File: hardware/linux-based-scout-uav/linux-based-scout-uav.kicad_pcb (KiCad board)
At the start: 2 copper layers, 39.4 x 59.1 mm, 3 parts, among them J1 XT60PW-M, J2 Micro_SD_Card_Det2, U1 OSD32MP157C-512M-IAA

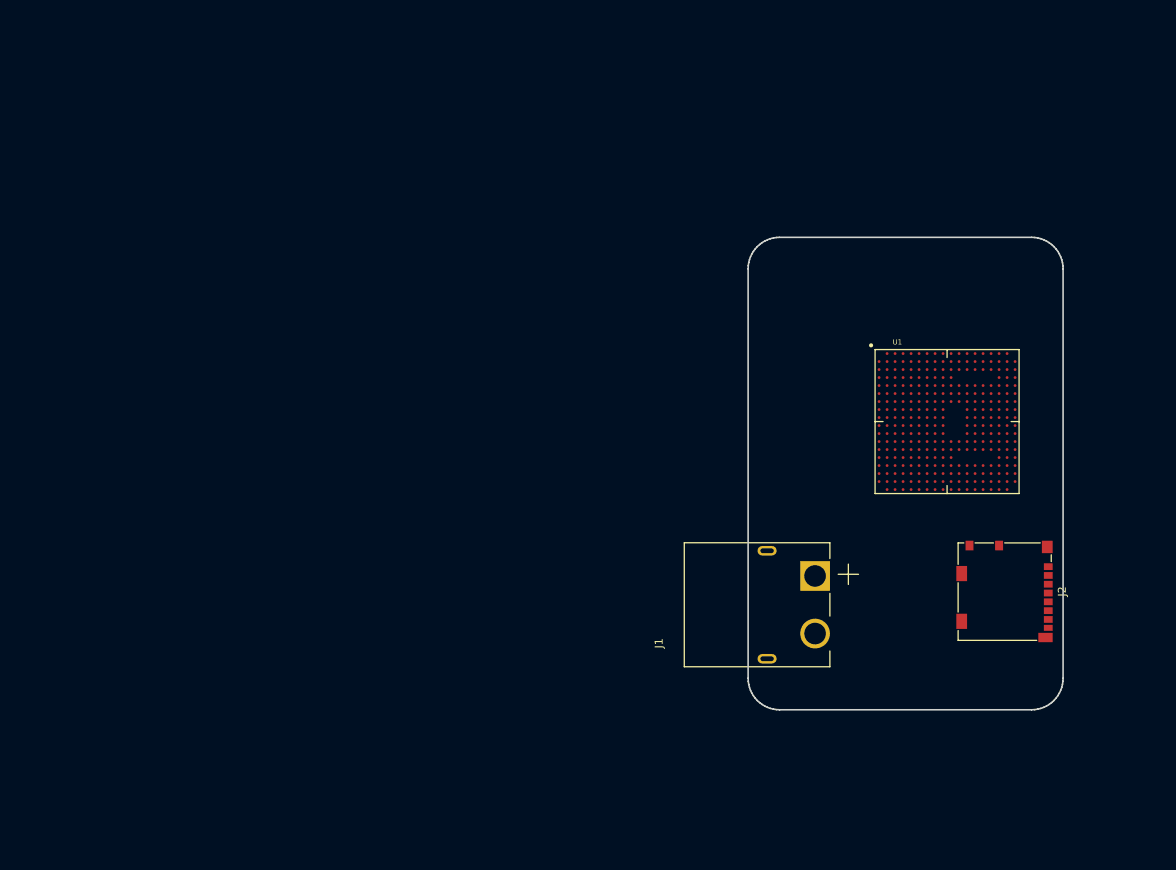
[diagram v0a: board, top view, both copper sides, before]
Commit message: Schematic, board update
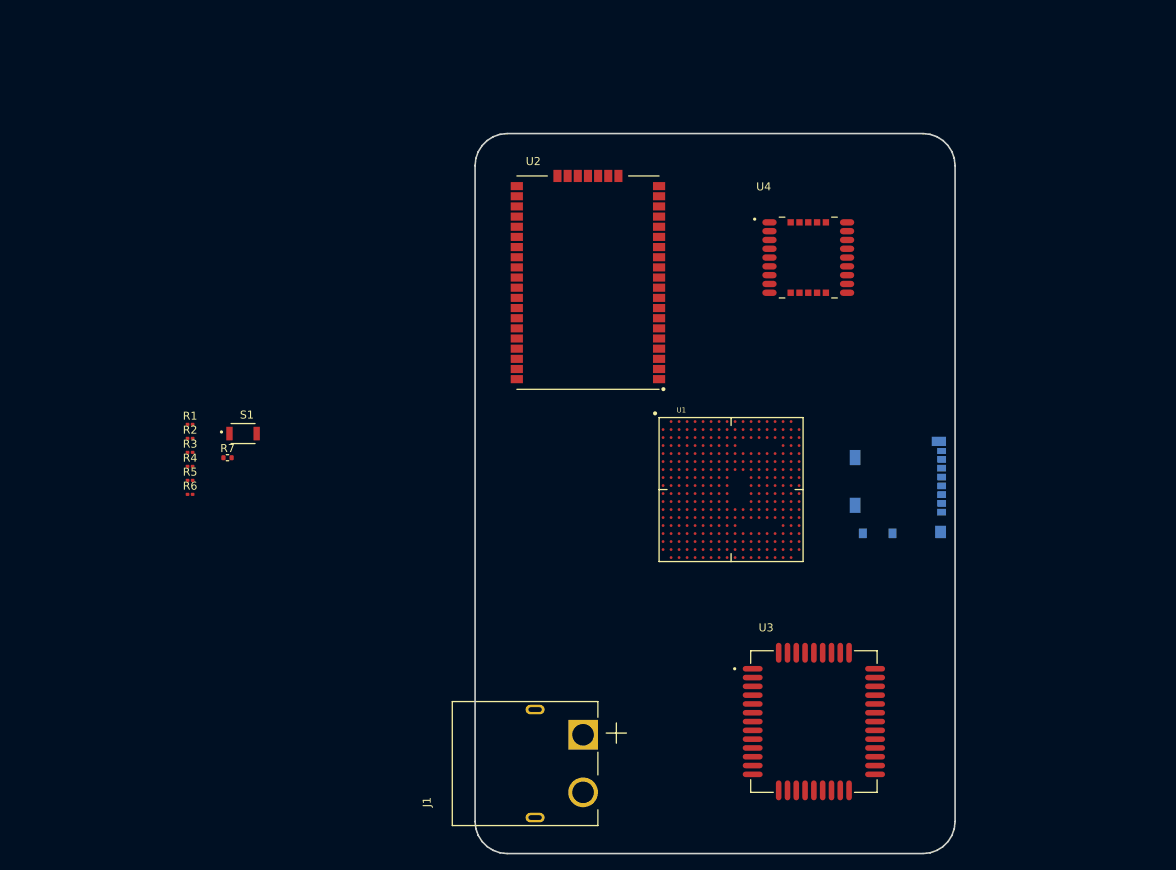
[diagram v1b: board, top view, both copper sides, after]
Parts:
- added R1: 10K, Resistor_SMD:R_0201_0603Metric, F.Cu at (93.4, 98.8)
- added R2: 10K, Resistor_SMD:R_0201_0603Metric, F.Cu at (93.4, 100.6)
- added R3: 10K, Resistor_SMD:R_0201_0603Metric, F.Cu at (93.4, 102.3)
- added R4: 10K, Resistor_SMD:R_0201_0603Metric, F.Cu at (93.4, 104.1)
- added R5: 10K, Resistor_SMD:R_0201_0603Metric, F.Cu at (93.4, 105.8)
- added R6: 10K, Resistor_SMD:R_0201_0603Metric, F.Cu at (93.4, 107.6)
- added R7: 10K, Resistor_SMD:R_0402_1005Metric, F.Cu at (98.1, 103.0)
- added S1: B3U-1000P, B3U-1000P:SW_B3U-1000P, F.Cu at (100.0, 100.0)
- added U2: RN2903A-I_RM098, RN2903A-I_RM098:XCVR_RN2903A-I_RM098, F.Cu at (143.1, 81.1)
- added U3: M65, M65:XCVR_M65, F.Cu at (171.3, 136.0)
- added U4: LC76G, LC76G:XCVR_LC76G, F.Cu at (170.7, 78.0)
- J2: moved to B.Cu
- moved J1 35.1 mm to (136.5, 141.2)
- moved U1 28.3 mm to (161.0, 107.0)
- moved J2 18.6 mm to (181.9, 106.7), turned to 90 degrees
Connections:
- net +5V renamed +VIN
- J2 pad 10: unconnected-(J2-DET_A-Pad10) -> GND
- J2 pad 11: unconnected-(J2-SHIELD-Pad11) -> GND
- J2 pad 3: unconnected-(J2-CMD-Pad3) -> SDMMC1_CMD
- J2 pad 4: unconnected-(J2-VDD-Pad4) -> +3V3
- J2 pad 5: unconnected-(J2-CLK-Pad5) -> SDMMC1_CK
- J2 pad 6: unconnected-(J2-VSS-Pad6) -> GND
- J2 pad 9: unconnected-(J2-DET_B-Pad9) -> ~SDDET
- U1 pad D3: unconnected-(U1A-PMIC_PONKEYN-PadD3) -> ~{PONKEY}
- U1 pad G6: unconnected-(U1A-BOOT2-PadG6) -> /osd32mp1-1-power/BOOT2
- U1 pad H3: unconnected-(U1A-PMIC_VOUT4_1-PadH3) -> +3V3
- U1 pad H6: unconnected-(U1A-BOOT1-PadH6) -> /osd32mp1-1-power/BOOT1
- U1 pad J3: unconnected-(U1A-PMIC_VOUT4_2-PadJ3) -> +3V3
- U1 pad J6: unconnected-(U1A-BOOT0-PadJ6) -> /osd32mp1-1-power/BOOT0
- U1 pad M10: unconnected-(U1A-BYPASS_REG1V8-PadM10) -> GND
- U1 pad U18: unconnected-(U1B-PD2-PadU18) -> SDMMC1_CMD
- U1 pad V17: unconnected-(U1B-PC12-PadV17) -> SDMMC1_CMD
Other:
- board size 39.4 x 59.1 mm -> 60 x 90 mm

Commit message: board, shchematic PDF update
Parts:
- J2: moved to F.Cu
- moved R1 23.0 mm to (115.7, 104.3)
- moved R2 23.0 mm to (115.7, 106.1)
- moved R3 23.0 mm to (115.7, 107.8)
- moved R4 23.0 mm to (115.7, 109.6)
- moved R5 23.0 mm to (115.7, 111.3)
- moved R6 23.0 mm to (115.7, 113.1)
- moved R7 23.0 mm to (120.4, 108.5)
- moved S1 23.0 mm to (122.3, 105.5)
- turned J2 to -90 degrees

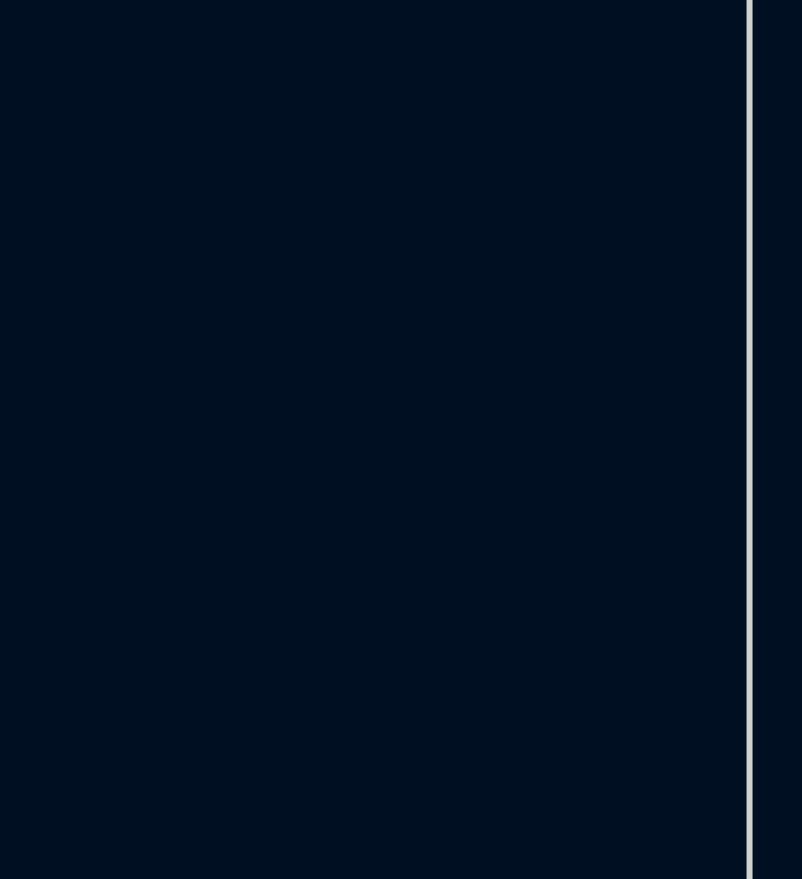
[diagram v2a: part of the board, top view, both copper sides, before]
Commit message: Shcematic, board update.
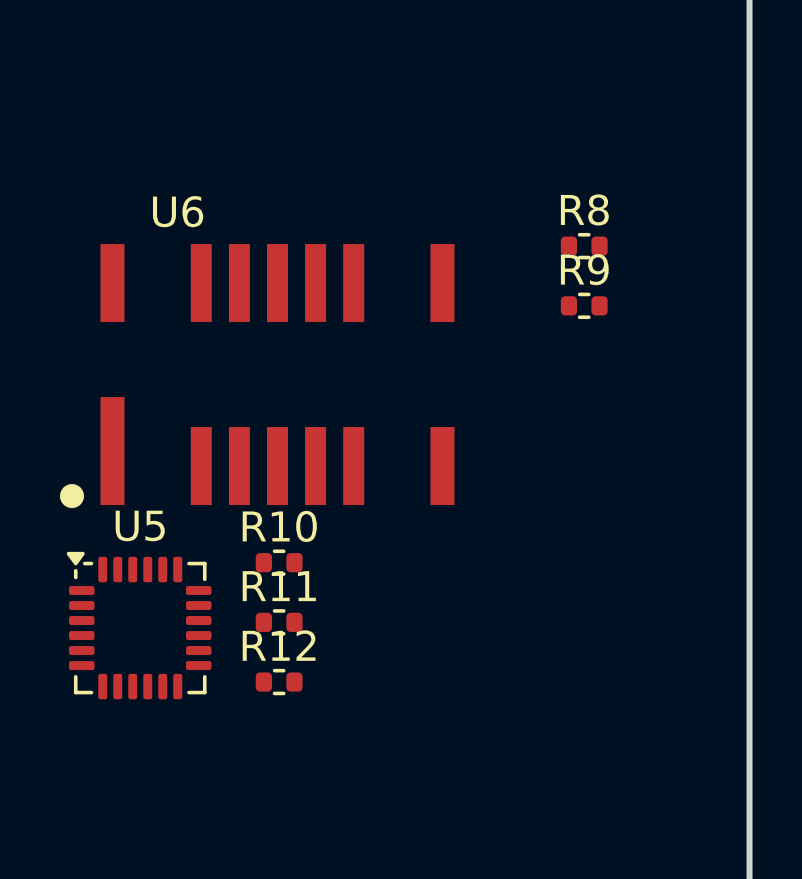
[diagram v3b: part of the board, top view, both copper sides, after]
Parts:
- added R10: 10K, Resistor_SMD:R_0402_1005Metric, F.Cu at (113.3, 91.1)
- added R11: 10K DNP, Resistor_SMD:R_0402_1005Metric, F.Cu at (113.3, 93.0)
- added R12: 10K DNP, Resistor_SMD:R_0402_1005Metric, F.Cu at (113.3, 95.0)
- added R8: Jumper, Resistor_SMD:R_0402_1005Metric, F.Cu at (123.5, 80.5)
- added R9: Jumper, Resistor_SMD:R_0402_1005Metric, F.Cu at (123.5, 82.5)
- added U5: MPU-6050, Sensor_Motion:InvenSense_QFN-24_4x4mm_P0.5mm, F.Cu at (108.7, 93.2)
- added U6: AMG8833, AMG8833:XDCR_AMG8833, F.Cu at (113.3, 84.8)
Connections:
- U1 pad G10: unconnected-(U1A-PMIC_SWOUT_2-PadG10) -> +VSW
- U1 pad G4: unconnected-(U1A-PMIC_LDO2-PadG4) -> +VLDO2
- U1 pad G7: unconnected-(U1A-VDD_1-PadG7) -> VDDI
- U1 pad G9: unconnected-(U1A-PMIC_SWOUT_1-PadG9) -> +VSW
- U1 pad H18: unconnected-(U1B-PB6-PadH18) -> I2C1_SCL
- U1 pad H7: unconnected-(U1A-VDD_2-PadH7) -> VDDI
- U1 pad J1: unconnected-(U1A-HSE_OSC_OEN-PadJ1) -> GND
- U1 pad J17: unconnected-(U1C-USB_DM2-PadJ17) -> USB_DM2
- U1 pad J18: unconnected-(U1C-USB_DP2-PadJ18) -> USB_DP2
- U1 pad J7: unconnected-(U1A-VDD_3-PadJ7) -> VDDI
- U1 pad J8: unconnected-(U1A-PMIC_BSTOUT_1-PadJ8) -> +BST
- U1 pad J9: unconnected-(U1A-PMIC_BSTOUT_2-PadJ9) -> +BST
- U1 pad K1: unconnected-(U1C-VSSA-PadK1) -> Net-(U1C-VSSA)
- U1 pad K17: unconnected-(U1C-USB_DP1-PadK17) -> USB_DP1
- U1 pad K18: unconnected-(U1C-USB_DM1-PadK18) -> USB_DM1
- U1 pad K2: unconnected-(U1C-VREF--PadK2) -> Net-(U1C-VREF-)
- U1 pad K4: unconnected-(U1A-VDD_7-PadK4) -> VDDI
- U1 pad K7: unconnected-(U1A-VDD_4-PadK7) -> VDDI
- U1 pad L4: unconnected-(U1A-VDD_8-PadL4) -> VDDI
- U1 pad L7: unconnected-(U1A-VDD_5-PadL7) -> VDDI
- U1 pad M1: unconnected-(U1C-VDDA-PadM1) -> Net-(U1C-VDDA)
- U1 pad M2: unconnected-(U1C-VREF+-PadM2) -> Net-(U1C-VREF+)
- U1 pad M3: unconnected-(U1A-NRST-PadM3) -> /osd32mp1-1-power/~{RESET}
- U1 pad M4: unconnected-(U1A-VDD_9-PadM4) -> VDDI
- U1 pad M7: unconnected-(U1A-VDD_6-PadM7) -> VDDI
- U1 pad P4: unconnected-(U1A-EEPROM_WP-PadP4) -> /osd32mp1-1-power/EEPROM_WP
- U1 pad R11: unconnected-(U1C-NJTRST-PadR11) -> /osd32mp1-2/~{TRST}
- U1 pad R12: unconnected-(U1C-JTDO-TRACESWO-PadR12) -> /osd32mp1-2/SWO/TDO
- U1 pad R13: unconnected-(U1C-JTDI-PadR13) -> /osd32mp1-2/TDI
- U1 pad R14: unconnected-(U1C-JTMS-SWDIO-PadR14) -> /osd32mp1-2/SWDIO/TMS
- U1 pad R15: unconnected-(U1C-JTCK-SWCLK-PadR15) -> /osd32mp1-2/SWCLK/TCK
- U1 pad V12: unconnected-(U1B-PB7-PadV12) -> I2C1_SDA
- U2 pad 1: Net-(U2-GND-Pad1) -> GND
- U2 pad 11: Net-(U2-GND-Pad1) -> GND
- U2 pad 20: Net-(U2-GND-Pad1) -> GND
- U2 pad 21: Net-(U2-GND-Pad1) -> GND
- U2 pad 22: Net-(U2-GND-Pad1) -> GND
- U2 pad 24: Net-(U2-GND-Pad1) -> GND
- U2 pad 26: Net-(U2-GND-Pad1) -> GND
- U2 pad 27: Net-(U2-GND-Pad1) -> GND
- U2 pad 28: Net-(U2-GND-Pad1) -> GND
- U2 pad 33: Net-(U2-GND-Pad1) -> GND
- U2 pad 41: Net-(U2-GND-Pad1) -> GND
- U2 pad 47: Net-(U2-GND-Pad1) -> GND
- U2 pad 8: Net-(U2-GND-Pad1) -> GND
- U3 pad 1: unconnected-(U3-AGND-Pad1) -> GND
- U3 pad 10: unconnected-(U3-SIM_GND-Pad10) -> GND
- U3 pad 27: Net-(U3-GND-Pad27) -> GND
- U3 pad 34: Net-(U3-GND-Pad27) -> GND
- U3 pad 36: Net-(U3-GND-Pad27) -> GND
- U3 pad 37: Net-(U3-GND-Pad27) -> GND
- U3 pad 40: Net-(U3-GND-Pad27) -> GND
- U3 pad 41: Net-(U3-GND-Pad27) -> GND
- U4 pad 1: Net-(U4-GND-Pad1) -> GND
- U4 pad 10: Net-(U4-GND-Pad1) -> GND
- U4 pad 12: Net-(U4-GND-Pad1) -> GND
- U4 pad 28: Net-(U4-GND-Pad1) -> GND

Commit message: Schematic update
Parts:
- added C1: 12pF, Capacitor_SMD:C_0402_1005Metric, F.Cu at (96.6, 135.4)
- added C2: 12pF, Capacitor_SMD:C_0402_1005Metric, F.Cu at (96.6, 137.3)
- added C3: 100nF, Capacitor_SMD:C_0402_1005Metric, F.Cu at (194.5, 125.5)
- added J3: TC2050-IDC-NL, TC2050-IDC-NL:TAG-CONNECT_TC2050-IDC-NL, F.Cu at (133.2, 117.0)
- added J4: 0786463001, 0786463001:MOLEX_0786463001, B.Cu at (180.5, 121.0)
- added L1: L, Inductor_SMD:L_0402_1005Metric, F.Cu at (101.8, 143.7)
- added R13: 22R, Resistor_SMD:R_0402_1005Metric, F.Cu at (194.5, 119.5)
- added R14: 22R, Resistor_SMD:R_0402_1005Metric, F.Cu at (194.5, 121.5)
- added R15: 22R, Resistor_SMD:R_0402_1005Metric, F.Cu at (194.5, 123.5)
- added U7: SX1272, Package_DFN_QFN:QFN-28-1EP_6x6mm_P0.65mm_EP4.8x4.8mm_ThermalVias, F.Cu at (137.6, 91.4)
- added Y1: ABS05-32.768KHZ-7-T, ABS05-32.768KHZ-7-T:XTAL_ABS05-32.768KHZ-7-T, F.Cu at (96.8, 139.6)
- U6: moved to B.Cu
- moved U5 50.9 mm to (159.5, 97.0)
- moved U2 43.6 mm to (103.0, 64.0)
- moved U6 38.4 mm to (144.6, 107.0), turned to -90 degrees
- moved U4 8.60 mm to (177.7, 73.0)
- moved U1 6.00 mm to (161.0, 113.0)
- moved U3 1.04 mm to (172.3, 136.3), turned to -90 degrees
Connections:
- net /osd32mp1-1-power/~{RESET} renamed ~{RESET}
- R12 pad 1: unconnected-(R12-Pad1) -> AMG833_INT
- U1 pad N1: unconnected-(U1B-PC15-OSC32_OUT-PadN1) -> Net-(U1B-PC15-OSC32_OUT)
- U1 pad N2: unconnected-(U1B-PC14-OSC32_IN-PadN2) -> Net-(U1B-PC14-OSC32_IN)
- U3 pad 11: unconnected-(U3-SIM_DATA-Pad11) -> Net-(U3-SIM_DATA)
- U3 pad 12: unconnected-(U3-SIM_RST-Pad12) -> Net-(U3-SIM_RST)
- U3 pad 13: unconnected-(U3-SIM_CLK-Pad13) -> Net-(U3-SIM_CLK)
- U3 pad 14: unconnected-(U3-SIM_VDD-Pad14) -> /quectel-m65-1/SIM_VDD
- U6 pad 2: unconnected-(U6-SDA-Pad2) -> I2C1_SDA
- U6 pad 3: unconnected-(U6-SCL-Pad3) -> I2C1_SCL

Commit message: Schematic/board update
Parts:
- added J5: GSB1C41110SSHR, GSB1C41110SSHR:AMPHENOL_GSB1C41110SSHR, F.Cu at (77.9, 110.3)
- added Q1: DMP3013SFV, Package_SON:Diodes_PowerDI3333-8, F.Cu at (74.1, 117.2)
- added Q2: DMP3013SFV, Package_SON:Diodes_PowerDI3333-8, F.Cu at (74.1, 122.1)
- added R16: 10K, Resistor_SMD:R_0402_1005Metric, F.Cu at (95.4, 123.8)
- added R17: 10K, Resistor_SMD:R_0402_1005Metric, F.Cu at (95.4, 125.8)
- added U8: EMMC04G-W627-M06U, EMMC04G-W627-M06U:BGA153N50P14X14_1300X1150X100N, F.Cu at (93.2, 91.8)
- added U9: CYPD3177-24LQ, Package_DFN_QFN:QFN-24-1EP_4x4mm_P0.5mm_EP2.75x2.75mm, F.Cu at (74.0, 132.8)
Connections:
- R10 pad 1: unconnected-(R10-Pad1) -> +3V3
- U1 pad L1: unconnected-(U1C-ANA0-PadL1) -> Net-(U1C-ANA0)
- U1 pad L2: unconnected-(U1C-ANA1-PadL2) -> Net-(U1C-ANA1)
- U5 pad 13: unconnected-(U5-VDD-Pad13) -> +3V3

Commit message: Schematic/board update
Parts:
- moved U8 118.4 mm to (208.8, 117.8)
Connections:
- J2 pad 2: SDMCC1_D3 -> SDMMC1_D3
- R2 pad 2: SDMCC1_D3 -> SDMMC1_D3
- U1 pad R16: unconnected-(U1B-PC7-PadR16) -> MMC2_D7
- U1 pad T14: unconnected-(U1B-PB14-PadT14) -> MMC2_D0
- U1 pad T17: unconnected-(U1B-PA8-PadT17) -> MMC2_D4
- U1 pad U12: unconnected-(U1B-PA9-PadU12) -> MMC2_D5
- U1 pad U14: unconnected-(U1B-PB4-PadU14) -> MMC2_D3
- U1 pad V13: unconnected-(U1B-PB15-PadV13) -> MMC2_D1
- U1 pad V14: unconnected-(U1B-PB3-PadV14) -> MMC2_D2
- U1 pad V15: unconnected-(U1D-PE5-PadV15) -> MMC2_D6
- U8 pad A3: /storage/MMC2_D0 -> MMC2_D0
- U8 pad A4: /storage/MMC2_D1 -> MMC2_D1
- U8 pad A5: /storage/MMC2_D2 -> MMC2_D2
- U8 pad B2: /storage/MMC2_D3 -> MMC2_D3
- U8 pad B3: /storage/MMC2_D4 -> MMC2_D4
- U8 pad B4: /storage/MMC2_D5 -> MMC2_D5
- U8 pad B5: /storage/MMC2_D6 -> MMC2_D6
- U8 pad B6: /storage/MMC2_D7 -> MMC2_D7
